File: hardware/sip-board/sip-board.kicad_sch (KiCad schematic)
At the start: 1 part, among them IC1 XC7S15-1CPGA196C

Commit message: wire up LDOs
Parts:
- added C1, C3, C6: 1u, symbol Device:C_Small
- added C2, C4, C5: 10u, symbol Device:C_Small
- added U1: TLV75710PDBV, Package_TO_SOT_SMD:SOT-23-5, symbol Regulator_Linear:TLV75710PDBV
- added U2: TLV75718PDBV, Package_TO_SOT_SMD:SOT-23-5, symbol Regulator_Linear:TLV75718PDBV
- added U3: TLV75733PDBV, Package_TO_SOT_SMD:SOT-23-5, symbol Regulator_Linear:TLV75733PDBV
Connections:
- net VCCINT is gone; now on net +1V0: IC1.E7 (VCCINT_1), IC1.E9 (VCCINT_2), IC1.F6 (VCCINT_3), IC1.G9 (VCCINT_4), IC1.H6 (VCCINT_5), IC1.J9 (VCCINT_6), IC1.K6 (VCCINT_7), IC1.K8 (VCCINT_8)
- net GND: now also C1.2, C2.2, C3.2, C4.2, C5.2, C6.2, U1.2 (GND), U2.2 (GND), U3.2 (GND)
- net +1V0: now reaches IC1.C7 (VCCBRAM_1)
- net +1V0: now also IC1.C9 (VCCBRAM_2), C1.1, U1.5 (OUT)
- net +1V8: now reaches IC1.D10 (VCCAUX_3)
- net +1V8: now also IC1.D6 (VCCAUX_1), IC1.D8 (VCCAUX_2), C3.1, C6.1, U2.5 (OUT), U3.5 (OUT)
- new net +5V: C2.1, C4.1, C5.1, U1.1 (IN), U1.3 (EN), U2.1 (IN), U2.3 (EN), U3.1 (IN), U3.3 (EN)
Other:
- note added: "5V -> 1.0V LDO: 2.9mm x 2.8mm"
- note added: "5V -> 1.8V LDO: 2.9mm x 2.8mm"
- note added: "5V -> 3.3V LDO: 2.9mm x 2.8mm"
- note added: "5V -> X.X LDOs"
- moved on the sheet: IC1

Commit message: boot config and spi eeprom
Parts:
- removed U1: TLV75710PDBV, Package_TO_SOT_SMD:SOT-23-5, symbol Regulator_Linear:TLV75710PDBV
- removed U2: TLV75718PDBV, Package_TO_SOT_SMD:SOT-23-5, symbol Regulator_Linear:TLV75718PDBV
- removed U3: TLV75733PDBV, Package_TO_SOT_SMD:SOT-23-5, symbol Regulator_Linear:TLV75733PDBV
- added R1, R2, R3: 1k, symbol Device:R_Small
- added R4: 2k4, symbol Device:R_Small
- added R5: 4k7, symbol Device:R_Small
- added SW1: SW_DIP_x03, symbol Switch:SW_DIP_x03
- added U1: M95256-WMN6P, Package_SO:SOIC-8_3.9x4.9mm_P1.27mm, symbol Memory_EEPROM:M95256-WMN6P
- added U2: TLV75710PDRV, Package_SON:WSON-6-1EP_2x2mm_P0.65mm_EP1x1.6mm, symbol Regulator_Linear:TLV75710PDRV
- added U3: TLV75718PDRV, Package_SON:WSON-6-1EP_2x2mm_P0.65mm_EP1x1.6mm, symbol Regulator_Linear:TLV75718PDRV
- added U4: TLV75733PDRV, Package_SON:WSON-6-1EP_2x2mm_P0.65mm_EP1x1.6mm, symbol Regulator_Linear:TLV75733PDRV
- C6: value 1u -> 100u
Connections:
- net +1V0: now also U2.1 (OUT)
- net +1V8: now also U3.1 (OUT); no longer C6.1
- net +5V: now also U2.4 (EN), U2.6 (IN), U3.4 (EN), U3.6 (IN), U4.4 (EN), U4.6 (IN)
- net GND: now also IC1.B10 (IO_L3P_T0_DQS_PUDC_B_14), R1.2, R2.2, R3.2, U1.4 (VSS), U2.3 (GND), U2.7 (GND), U3.3 (GND), U3.7 (GND), U4.3 (GND), U4.7 (GND)
- net CCLK: now reaches IC1.A7 (CCLK_0)
- net CCLK: now also U1.6 (C)
- net TCK: now reaches IC1.A8 (TCK_0)
- net MOSI: now reaches IC1.C10 (IO_L1P_T0_D00_MOSI_14)
- net MOSI: now also U1.5 (D)
- net DIN: now reaches IC1.C11 (IO_L1N_T0_D01_DIN_14)
- net DIN: now also U1.2 (Q)
- net CS: now reaches IC1.D13 (IO_L6P_T0_FCS_B_14)
- net CS: now also R4.2, U1.1 (~{S})
- net +3.3V: now reaches IC1.E5 (VCCO_34_1)
- net +3.3V: now also C6.1, IC1.F10 (VCCO_14_1), IC1.G5 (VCCO_34_2), IC1.H10 (VCCO_14_2), IC1.K10 (VCCO_14_3), IC1.N6 (VCCO_0_1), IC1.N9 (CFGBVS_0), IC1.P8 (VCCO_0_2), R4.1, R5.1, SW1.1, SW1.2, SW1.3, U1.3 (~{W}), U1.7 (~{HOLD}), U1.8 (VCC), U4.1 (OUT)
- net M0_CONFIG: now reaches IC1.L10 (M0_0)
- net M0_CONFIG: now also R1.1, SW1.4
- net TMS: now reaches IC1.L7 (TMS_0)
- net M1_CONFIG: now reaches IC1.L8 (M1_0)
- net M1_CONFIG: now also R2.1, SW1.5
- net M2_CONFIG: now reaches IC1.L9 (M2_0)
- net M2_CONFIG: now also R3.1, SW1.6
- net TDO: now reaches IC1.M6 (TDO_0)
- net TDI: now reaches IC1.M7 (TDI_0)
- net DONE: now reaches IC1.M9 (DONE_0)
- net at IC1.N7 (INIT_B_0): now also R5.2
- net PROGRAM_B: now reaches IC1.N8 (PROGRAM_B_0)
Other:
- note added: "5V -> 1.0V VCCINT LDO: 2x2 mm"
- note added: "5V -> 1.8V VCCAUX LDO: 2x2 mm"
- note added: "5V -> 3.3V VCCO LDO: 2x2 mm"
- note added: "5V -> X.X LDOs WSON-6 package"
- note added: "Boot Configuration"
- note added: "Configuration Banks Voltage Select section in the config user guide"
- note added: "SPI PROM 3.9mm x 4.9mm We are configuring FPGA from SPI - see Config UG"
- note added: "XC7 PCB guide https://docs.amd.com/v/u/en-US/ug483_7Series_PCB XC7 Config https://docs.amd.com/v/u/en-US/ug470_7Series_Config"
- note removed: "5V -> 1.0V LDO: 2.9mm x 2.8mm"
- note removed: "5V -> 1.8V LDO: 2.9mm x 2.8mm"
- note removed: "5V -> 3.3V LDO: 2.9mm x 2.8mm"
- note removed: "5V -> X.X LDOs"
- note removed: "XC7 PCB guide https://docs.amd.com/v/u/en-US/ug483_7Series_PCB"
- moved on the sheet: IC1

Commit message: jtag connector, decoupling caps, level shifters on schematic
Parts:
- added C10, C11, C14, C17, C18, C19, C20, C24, C25, C26, C27, C28, C29, C33, C34, C35, C36: 0.47u, Capacitor_SMD:C_0201_0603Metric, symbol Device:C_Small
- added C12, C15: 47u, Capacitor_SMD:C_0201_0603Metric, symbol Device:C_Small
- added C13, C16, C22, C23, C31, C32, C38, C39, C8, C9: 4.7u, Capacitor_SMD:C_0201_0603Metric, symbol Device:C_Small
- added C21, C30, C37, C7: 100u, Capacitor_SMD:C_0201_0603Metric, symbol Device:C_Small
- added D1: D_Small, Diode_SMD:D_0201_0603Metric, symbol Device:D_Small
- added J1: Conn_01x06_Pin, Connector_PinHeader_2.54mm:PinHeader_1x06_P2.54mm_Vertical, symbol Connector:Conn_01x06_Pin
- added J2, J3, J4, J5: Conn_01x10_Pin, Connector_PinHeader_2.54mm:PinHeader_1x10_P2.54mm_Vertical, symbol Connector:Conn_01x10_Pin
- added R10, R11, R12, R13, R14, R15, R6, R7, R8, R9: 10k, Resistor_SMD:R_0201_0603Metric, symbol Device:R_Small
- added U10, U11, U12, U13, U14, U5, U6, U7, U8, U9: ~, hardware:NXB0104_XQFN12, symbol custom_symbols:NXB0104_XQFN12
- C1, C2, C3, C6: footprint (none) -> Capacitor_SMD:C_0201_0603Metric
- C4, C5: value 10u -> 50u; footprint (none) -> Capacitor_SMD:C_0201_0603Metric
- IC1: footprint BGA196C50P14X14_800X800X110 -> fpga_stuff:BGA196C50P14X14_800X800X110
- R1, R2, R3, R4, R5: footprint (none) -> Resistor_SMD:R_0201_0603Metric
- SW1: footprint (none) -> Button_Switch_SMD:SW_DIP_SPSTx03_Slide_6.7x9.18mm_W6.73mm_P2.54mm_LowProfile_JPin
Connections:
- net +1V0: now also C10.1, C11.1, C12.1, C13.1, C14.1, C7.1, C8.1, C9.1
- net +1V8: now also C15.1, C16.1, C17.1, C18.1
- net +3.3V: now also C19.1, C20.1, C21.1, C22.1, C23.1, C24.1, C25.1, C26.1, C27.1, C28.1, C29.1, C30.1, C31.1, C32.1, C33.1, C34.1, C35.1, C36.1, C37.1, C38.1, C39.1, D1.1 (K)
- net +5V: now also J3.1 (Pin_1), U10.12 (VCC_B), U11.12 (VCC_B), U12.12 (VCC_B), U13.12 (VCC_B), U14.12 (VCC_B), U5.12 (VCC_B), U6.12 (VCC_B), U7.12 (VCC_B), U8.12 (VCC_B), U9.12 (VCC_B)
- net CCLK: now also J1.3 (Pin_3)
- net CS: now also J1.6 (Pin_6)
- net GND: now also IC1.J7 (DXN_0), IC1.J8 (DXP_0), C10.2, C11.2, C12.2, C13.2, C14.2, C15.2, C16.2, C17.2, C18.2, C19.2, C20.2, C21.2, C22.2, C23.2, C24.2, C25.2, C26.2, C27.2, C28.2, C29.2, C30.2, C31.2, C32.2, C33.2, C34.2, C35.2, C36.2, C37.2, C38.2, C39.2, C7.2, C8.2, C9.2, J1.2 (Pin_2), J4.9 (Pin_9), U10.6 (GND), U11.6 (GND), U12.6 (GND), U13.6 (GND), U14.6 (GND), U5.6 (GND), U6.6 (GND), U7.6 (GND), U8.6 (GND), U9.6 (GND)
- net MOSI: now also J1.4 (Pin_4)
- net TDI: now also J1.5 (Pin_5)
- new net: R10.2, U9.7 (OE)
- new net: R14.2, U13.7 (OE)
- new net: R7.2, U6.7 (OE)
- new net: R12.2, U11.7 (OE)
- new net: R15.2, U14.7 (OE)
- new net: R8.2, U7.7 (OE)
- new net: R11.2, U10.7 (OE)
- new net: R13.2, U12.7 (OE)
- new net: R9.2, U8.7 (OE)
- new net: R6.2, U5.7 (OE)
- new net +3V3: R10.1, R11.1, R12.1, R13.1, R14.1, R15.1, R6.1, R7.1, R8.1, R9.1, U10.1 (VCC_A), U11.1 (VCC_A), U12.1 (VCC_A), U13.1 (VCC_A), U14.1 (VCC_A), U5.1 (VCC_A), U6.1 (VCC_A), U7.1 (VCC_A), U8.1 (VCC_A), U9.1 (VCC_A)
- new net A0_5V: J4.10 (Pin_10), U12.10 (B2)
- new net A0_FPGA: U12.3 (A2)
- new net A10_5V: J5.10 (Pin_10), U14.8 (B4)
- new net A10_FPGA: U14.5 (A4)
- new net A11_5V: J2.1 (Pin_1), U5.11 (B1)
- new net A11_FPGA: U5.2 (A1)
- new net A12_5V: J2.2 (Pin_2), U5.10 (B2)
- new net A12_FPGA: U5.3 (A2)
- new net A13_5V: J2.3 (Pin_3), U5.9 (B3)
- new net A13_FPGA: U5.4 (A3)
- new net A14_5V: J2.4 (Pin_4), U5.8 (B4)
- new net A14_FPGA: U5.5 (A4)
- new net A15_5V: J2.5 (Pin_5), U6.11 (B1)
- new net A15_FPGA: U6.2 (A1)
- new net A1_5V: J5.1 (Pin_1), U12.9 (B3)
- new net A1_FPGA: U12.4 (A3)
- new net A2_5V: J5.2 (Pin_2), U12.8 (B4)
- new net A2_FPGA: U12.5 (A4)
- new net A3_5V: J5.3 (Pin_3), U13.11 (B1)
- new net A3_FPGA: U13.2 (A1)
- new net A4_5V: J5.4 (Pin_4), U13.10 (B2)
- new net A4_FPGA: U13.3 (A2)
- new net A5_5V: J5.5 (Pin_5), U13.9 (B3)
- new net A5_FPGA: U13.4 (A3)
- new net A6_5V: J5.6 (Pin_6), U13.8 (B4)
- new net A6_FPGA: U13.5 (A4)
- new net A7_5V: J5.7 (Pin_7), U14.11 (B1)
- new net A7_FPGA: U14.2 (A1)
- new net A8_5V: J5.8 (Pin_8), U14.10 (B2)
- new net A8_FPGA: U14.3 (A2)
- new net A9_5V: J5.9 (Pin_9), U14.9 (B3)
- new net A9_FPGA: U14.4 (A3)
- new net BUSAK_5V: J4.3 (Pin_3), U10.9 (B3)
- new net BUSAK_FPGA: U10.4 (A3)
- new net BUSRQ_5V: J4.5 (Pin_5), U11.11 (B1)
- new net BUSRQ_FPGA: U11.2 (A1)
- new net CLK: U6.3 (A2)
- new net CLK_5V: J2.6 (Pin_6), U6.10 (B2)
- new net D0_5V: J3.4 (Pin_4), U8.10 (B2)
- new net D0_FPGA: U8.3 (A2)
- new net D1_5V: J3.5 (Pin_5), U8.9 (B3)
- new net D1_FPGA: U8.4 (A3)
- new net D2_5V: J3.2 (Pin_2), U7.8 (B4)
- new net D2_FPGA: U7.5 (A4)
- new net D3_5V: J2.8 (Pin_8), U6.8 (B4)
- new net D3_FPGA: U6.5 (A4)
- new net D4_5V: J2.7 (Pin_7), U6.9 (B3)
- new net D4_FPGA: U6.4 (A3)
- new net D5_5V: J2.9 (Pin_9), U7.11 (B1)
- new net D5_FPGA: U7.2 (A1)
- new net D6_5V: J2.10 (Pin_10), U7.10 (B2)
- new net D6_FPGA: U7.3 (A2)
- new net D7_5V: J3.3 (Pin_3), U8.11 (B1)
- new net D7_FPGA: U8.2 (A1)
- new net HALT_5V: J3.8 (Pin_8), U9.10 (B2)
- new net HALT_FPGA: U9.3 (A2)
- new net INT_5V: J3.6 (Pin_6), U8.8 (B4)
- new net INT_FPGA: U8.5 (A4)
- new net IORQ_5V: J3.10 (Pin_10), U9.8 (B4)
- new net IORQ_FPGA: U9.5 (A4)
- new net M1_5V: J4.7 (Pin_7), U11.9 (B3)
- new net M1_FPGA: U11.4 (A3)
- new net MREQ_5V: J3.9 (Pin_9), U9.9 (B3)
- new net MREQ_FPGA: U9.4 (A3)
- new net NMI_5V: J3.7 (Pin_7), U9.11 (B1)
- new net NMI_FPGA: U9.2 (A1)
- new net RD_5V: J4.1 (Pin_1), U10.11 (B1)
- new net RD_FPGA: U10.2 (A1)
- new net RESET_5V: J4.6 (Pin_6), U11.10 (B2)
- new net RESET_FPGA: U11.3 (A2)
- new net RFSH_5V: J4.8 (Pin_8), U11.8 (B4)
- new net RFSH_FPGA: U11.5 (A4)
- new net VDD: D1.2 (A), J1.1 (Pin_1)
- new net WAIT_5V: J4.4 (Pin_4), U10.8 (B4)
- new net WAIT_FPGA: U10.5 (A4)
- new net WR_5V: J4.2 (Pin_2), U10.10 (B2)
- new net WR_FPGA: U10.3 (A2)
- no-connect marks 7 -> 16
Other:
- note added: "3V3<->5V level shifters (FPGA <-> Z80 System)"
- note added: "Decoupling Capacitors"
- note added: "JTAG <-> SPI Thank you digilent. I love you. JTAG-HS1 Connector Note: DO NOT connect both JTAG and Z80 board at same time."
- note added: "PAGE 21 ONWARDS https://docs.amd.com/v/u/en-US/ug475_7Series_Pkg_Pinout"
- note added: "Pins 1-20 (ascending order)"
- note added: "Pins 21-40 (ascending order)"
- note added: "This A1 --> is GND on original Z80"
- note added: "This A3 --> is VCC (5V) on original Z80"
- note added: "We want pullup on OE"
- note added: "Z80 System Connectors PIN HEADERS!"
- note added: "https://docs.amd.com/v/u/en-US/ug483_7Series_PCB Page 14"
- moved on the sheet: IC1, R4, R5

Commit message: fix some connections, layout
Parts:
- removed C12: 47u, Capacitor_SMD:C_0201_0603Metric, symbol Device:C_Small
- removed C13: 4.7u, Capacitor_SMD:C_0201_0603Metric, symbol Device:C_Small
- removed C14: 0.47u, Capacitor_SMD:C_0201_0603Metric, symbol Device:C_Small
- added C40: 10u, Capacitor_SMD:C_0201_0603Metric, symbol Device:C_Small
- added R16: 5k, Resistor_SMD:R_0201_0603Metric, symbol Device:R_Small
- added SW2: SW_RESET, Button_Switch_SMD:SW_Push_1P1T_NO_6x6mm_H9.5mm, symbol Switch:SW_Push
- J1: footprint Connector_PinHeader_2.54mm:PinHeader_1x06_P2.54mm_Vertical -> Connector_PinHeader_2.54mm:PinHeader_1x06_P2.54mm_Vertical_SMD_Pin1Right
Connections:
- net +3.3V is gone; now on net +3V3: C19.1, C20.1, C21.1, C22.1, C23.1, C24.1, C25.1, C26.1, C27.1, C28.1, C29.1, C30.1, C31.1, C32.1, C33.1, C34.1, C35.1, C36.1, C37.1, C38.1, C39.1, C6.1, D1.1 (K), IC1.E5 (VCCO_34_1), IC1.F10 (VCCO_14_1), IC1.G5 (VCCO_34_2), IC1.H10 (VCCO_14_2), IC1.K10 (VCCO_14_3), IC1.N6 (VCCO_0_1), IC1.N9 (CFGBVS_0), IC1.P8 (VCCO_0_2), R4.1, R5.1, SW1.1, SW1.2, SW1.3, U1.3 (~{W}), U1.7 (~{HOLD}), U1.8 (VCC), U4.1 (OUT)
- net TCK is gone; now on net CCLK: IC1.A8 (TCK_0)
- net TDI is gone; now on net MOSI: IC1.M7 (TDI_0), J1.5 (Pin_5)
- net TMS is gone; now on net CS: IC1.L7 (TMS_0)
- net +3V3: now also R16.1
- net GND: now also C40.2
- net MOSI: no longer J1.4 (Pin_4)
- net PROGRAM_B: now also R16.2, SW2.1
- net TDO: now also J1.4 (Pin_4)
- new net: C40.1, SW2.2
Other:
- note added: "Reset Logic"
- note added: "https://docs.amd.com/r/en-US/ug1099-bga-device-design-rules/Power-Delivery-to-the-FPGA"

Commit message: redid part of the board
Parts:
- added D2, D3, D4, D5, D6: LED, LED_SMD:LED_0201_0603Metric, symbol Device:LED
- added R17, R20: 5k7, Resistor_SMD:R_0201_0603Metric, symbol Device:R_Small
- added R18: 2k3, Resistor_SMD:R_0201_0603Metric, symbol Device:R_Small
- added R19: 3k, Resistor_SMD:R_0201_0603Metric, symbol Device:R_Small
- renumbered C2 to C1, C19 to C10, C40 to C11, C10 to C12, C20 to C13, C7 to C14, C21 to C15, C8 to C16, C22 to C17, C9 to C18, C23 to C19, C4 to C2, C26 to C20, C27 to C21, C28 to C22, C29 to C23, C15 to C24, C30 to C25, C16 to C26, C31 to C27, C17 to C28, C32 to C29, C5 to C3, C18 to C30, C33 to C31, C34 to C32, C35 to C33, C36 to C34, C37 to C35, C38 to C36, C39 to C37, C3 to C4, C6 to C5, C1 to C6, C25 to C7, C24 to C8, C11 to C9, R12 to R10, R13 to R11, R14 to R12, R15 to R13, R16 to R14, R4 to R15, R5 to R16, R6 to R4, R7 to R5, R8 to R6, R9 to R7, R10 to R8, R11 to R9, U3 to U1, U4 to U2, U2 to U3, U1 to U4
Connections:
- net +1V0: now also R18.2
- net +1V8: now also R19.2
- net +3V3: now also D6.1 (K), R20.2; no longer R16.1
- net DONE: now also R17.1
- net GND: now also D2.1 (K), D3.1 (K), D4.1 (K), D5.1 (K)
- new net: D5.2 (A), R20.1
- new net: D6.2 (A), R16.1
- new net: D2.2 (A), R17.2
- new net: D3.2 (A), R18.1
- new net: D4.2 (A), R19.1

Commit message: files
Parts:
- J2, J3, J4, J5: now not fitted; now left out of the parts list
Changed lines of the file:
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@@
 		(unit 1)
 		(exclude_from_sim no)
-		(in_bom yes)
+		(in_bom no)
 		(on_board yes)
-		(dnp no)
+		(dnp yes)
 		(property "Reference" "J2"
 			(at 36.195 513.08 0)
@@
 		(unit 1)
 		(exclude_from_sim no)
-		(in_bom yes)
+		(in_bom no)
 		(on_board yes)
-		(dnp no)
+		(dnp yes)
 		(property "Reference" "J3"
 			(at 36.195 538.48 0)
@@
 		(unit 1)
 		(exclude_from_sim no)
-		(in_bom yes)
+		(in_bom no)
 		(on_board yes)
-		(dnp no)
+		(dnp yes)
 		(property "Reference" "J5"
 			(at 73.025 538.48 0)
@@
 		(unit 1)
 		(exclude_from_sim no)
-		(in_bom yes)
+		(in_bom no)
 		(on_board yes)
-		(dnp no)
+		(dnp yes)
 		(property "Reference" "J4"
 			(at 73.025 513.08 0)

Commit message: wip layout, part placement
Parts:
- J1: footprint Connector_PinHeader_2.54mm:PinHeader_1x06_P2.54mm_Vertical_SMD_Pin1Right -> Connector_PinHeader_2.54mm:PinHeader_1x06_P2.54mm_Vertical_SMD_Pin1Left
- renumbered SW1 to CFG1, D2 to DONE1, D6 to INIT1, U4 to SPIPROM1
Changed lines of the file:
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@@
 		(dnp no)
 		(fields_autoplaced yes)
-		(property "Reference" "SW1"
+		(property "Reference" "CFG1"
 			(at 38.1 148.59 0)
 			(effects
@@
 			(project "sip-board"
 				(path "/4eae758a-da4d-4448-84d4-770db7217b0d"
-					(reference "SW1")
+					(reference "CFG1")
 					(unit 1)
 				)
@@
 		(dnp no)
 		(fields_autoplaced yes)
-		(property "Reference" "D2"
+		(property "Reference" "DONE1"
 			(at 292.4175 93.98 0)
 			(effects
@@
 			(project "sip-board"
 				(path "/4eae758a-da4d-4448-84d4-770db7217b0d"
-					(reference "D2")
+					(reference "DONE1")
 					(unit 1)
 				)
@@
 		(dnp no)
 		(fields_autoplaced yes)
-		(property "Reference" "U4"
+		(property "Reference" "SPIPROM1"
 			(at 47.9141 195.58 0)
 			(effects
@@
 			(project "sip-board"
 				(path "/4eae758a-da4d-4448-84d4-770db7217b0d"
-					(reference "U4")
+					(reference "SPIPROM1")
 					(unit 1)
 				)
@@
 			)
 		)
-		(property "Footprint" "Connector_PinHeader_2.54mm:PinHeader_1x06_P2.54mm_Vertical_SMD_Pin1Right"
+		(property "Footprint" "Connector_PinHeader_2.54mm:PinHeader_1x06_P2.54mm_Vertical_SMD_Pin1Left"
 			(at 21.59 240.03 0)
 			(effects
@@
 		(dnp no)
 		(fields_autoplaced yes)
-		(property "Reference" "D6"
+		(property "Reference" "INIT1"
 			(at 1040.13 301.9424 90)
 			(effects
@@
 			(project "sip-board"
 				(path "/4eae758a-da4d-4448-84d4-770db7217b0d"
-					(reference "D6")
+					(reference "INIT1")
 					(unit 1)
 				)

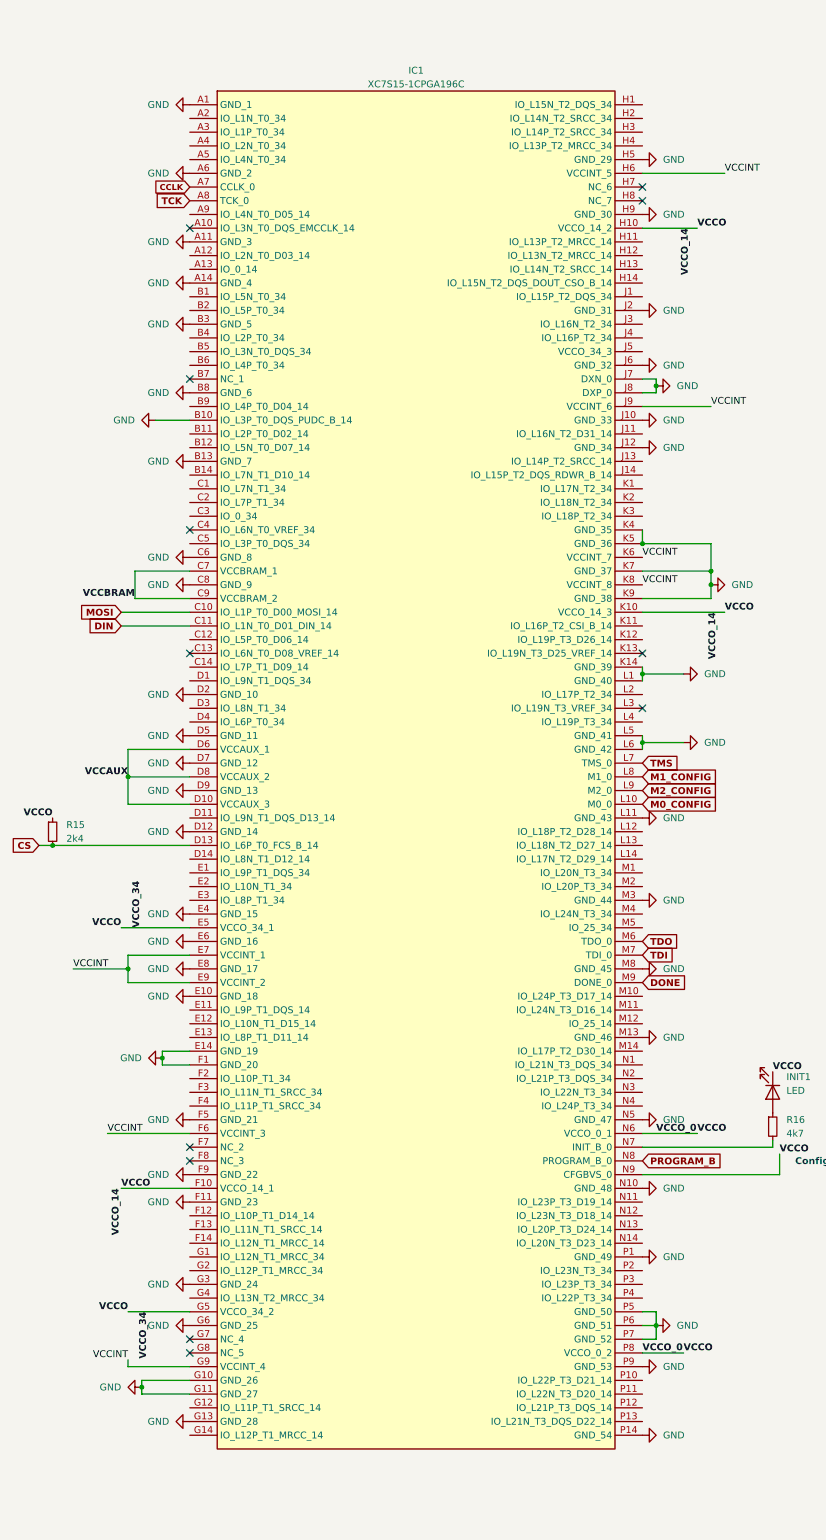
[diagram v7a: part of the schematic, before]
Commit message: Finish draft 1(.5?) of SiP board. Needs to be looked at again and probably redone.
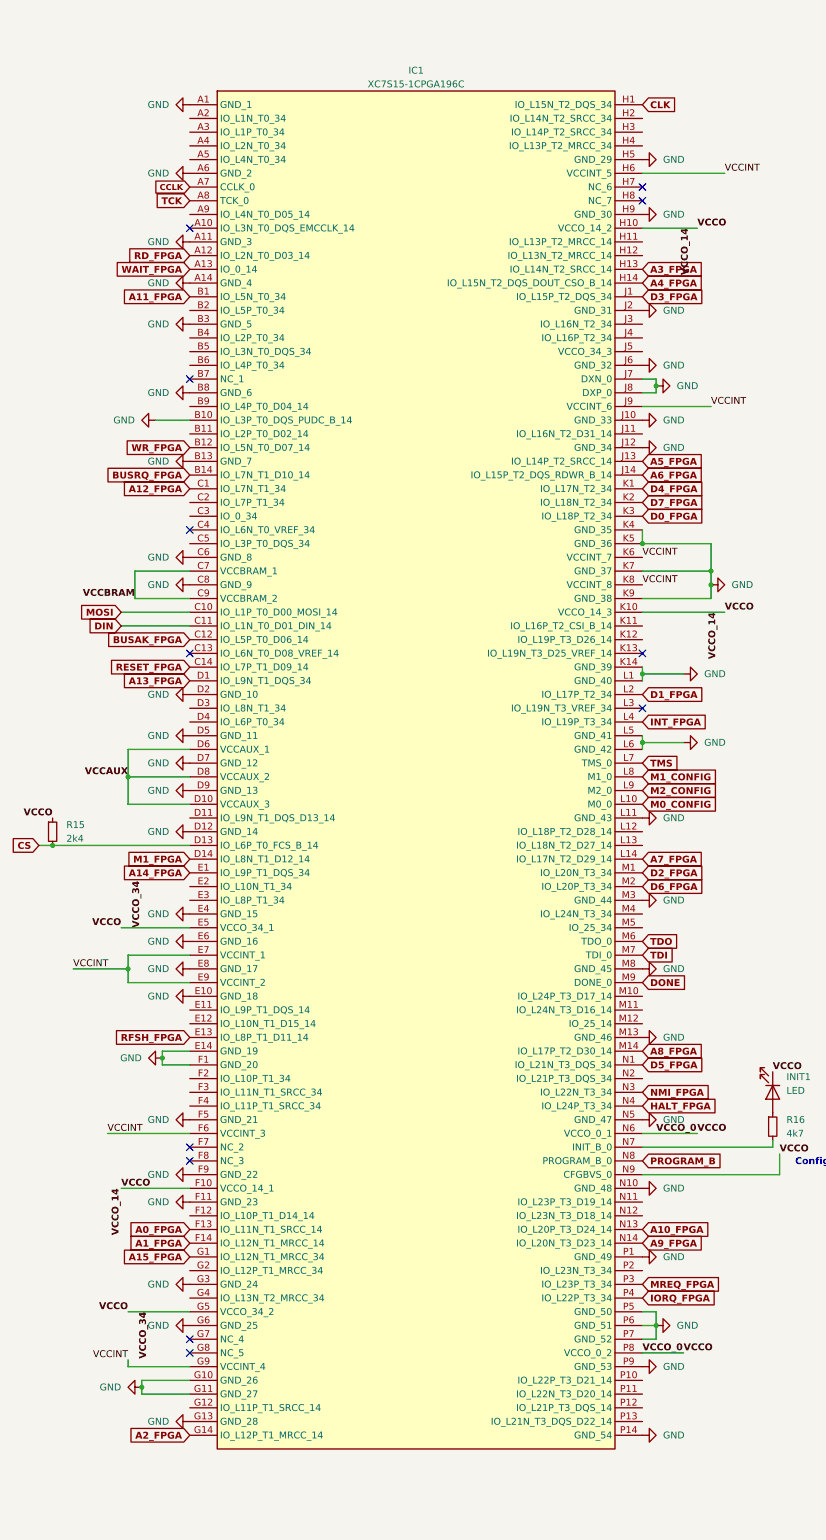
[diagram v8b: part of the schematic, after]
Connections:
- net A0_FPGA: now also IC1.F13 (IO_L11N_T1_SRCC_14)
- net A10_FPGA: now also IC1.N13 (IO_L20P_T3_D24_14)
- net A11_FPGA: now also IC1.B1 (IO_L5N_T0_34)
- net A12_FPGA: now also IC1.C1 (IO_L7N_T1_34)
- net A13_FPGA: now also IC1.D1 (IO_L9N_T1_DQS_34)
- net A14_FPGA: now also IC1.E1 (IO_L9P_T1_DQS_34)
- net A15_FPGA: now also IC1.G1 (IO_L12N_T1_MRCC_34)
- net A1_FPGA: now also IC1.F14 (IO_L12N_T1_MRCC_14)
- net A2_FPGA: now also IC1.G14 (IO_L12P_T1_MRCC_14)
- net A3_FPGA: now also IC1.H13 (IO_L14N_T2_SRCC_14)
- net A4_FPGA: now also IC1.H14 (IO_L15N_T2_DQS_DOUT_CSO_B_14)
- net A5_FPGA: now also IC1.J13 (IO_L14P_T2_SRCC_14)
- net A6_FPGA: now also IC1.J14 (IO_L15P_T2_DQS_RDWR_B_14)
- net A7_FPGA: now also IC1.L14 (IO_L17N_T2_D29_14)
- net A8_FPGA: now also IC1.M14 (IO_L17P_T2_D30_14)
- net A9_FPGA: now also IC1.N14 (IO_L20N_T3_D23_14)
- net BUSAK_FPGA: now also IC1.C12 (IO_L5P_T0_D06_14)
- net BUSRQ_FPGA: now also IC1.B14 (IO_L7N_T1_D10_14)
- net CLK: now also IC1.H1 (IO_L15N_T2_DQS_34)
- net D0_FPGA: now also IC1.K3 (IO_L18P_T2_34)
- net D1_FPGA: now also IC1.L2 (IO_L17P_T2_34)
- net D2_FPGA: now also IC1.M1 (IO_L20N_T3_34)
- net D3_FPGA: now also IC1.J1 (IO_L15P_T2_DQS_34)
- net D4_FPGA: now also IC1.K1 (IO_L17N_T2_34)
- net D5_FPGA: now also IC1.N1 (IO_L21N_T3_DQS_34)
- net D6_FPGA: now also IC1.M2 (IO_L20P_T3_34)
- net D7_FPGA: now also IC1.K2 (IO_L18N_T2_34)
- net HALT_FPGA: now also IC1.N4 (IO_L24P_T3_34)
- net INT_FPGA: now also IC1.L4 (IO_L19P_T3_34)
- net IORQ_FPGA: now also IC1.P4 (IO_L22P_T3_34)
- net M1_FPGA: now also IC1.D14 (IO_L8N_T1_D12_14)
- net MREQ_FPGA: now also IC1.P3 (IO_L23P_T3_34)
- net NMI_FPGA: now also IC1.N3 (IO_L22N_T3_34)
- net RD_FPGA: now also IC1.A12 (IO_L2N_T0_D03_14)
- net RESET_FPGA: now also IC1.C14 (IO_L7P_T1_D09_14)
- net RFSH_FPGA: now also IC1.E13 (IO_L8P_T1_D11_14)
- net WAIT_FPGA: now also IC1.A13 (IO_0_14)
- net WR_FPGA: now also IC1.B12 (IO_L5N_T0_D07_14)
